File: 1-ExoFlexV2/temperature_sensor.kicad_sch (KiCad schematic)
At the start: 15 parts, among them J109 Jumper, J110 Jumper, U85 COMP, U86 COMP, U87 OR Gate

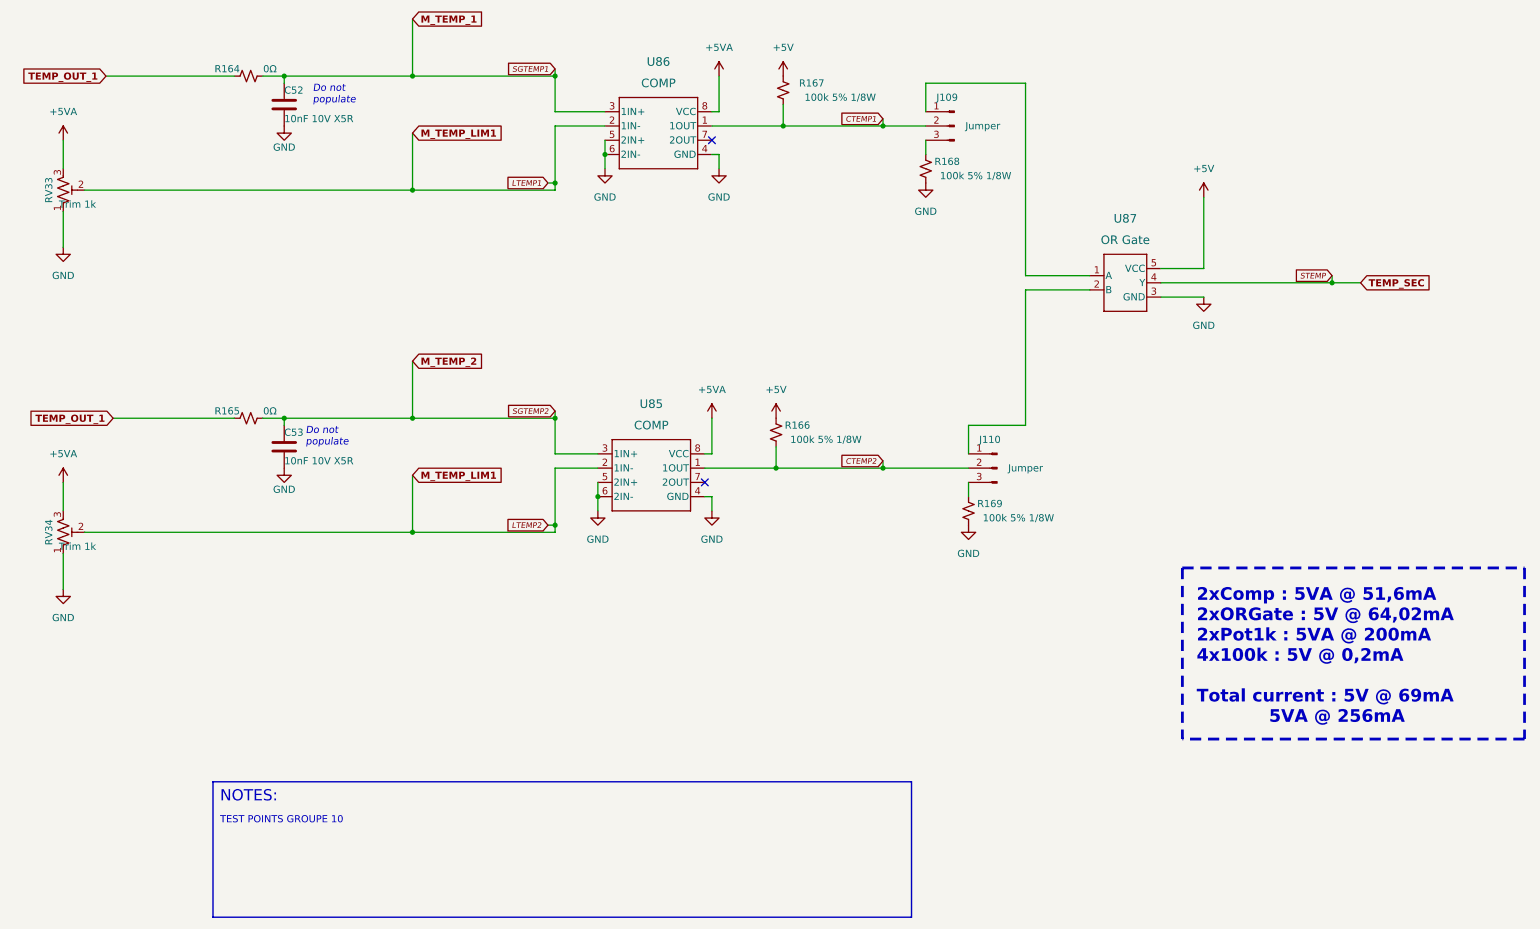
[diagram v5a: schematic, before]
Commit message: Finalisation 3
- Changement des régulateur de tension
- Retrait de test point inutile
- Changement de jumper mal positionner
- Ajout de Mounting holes et fiducial
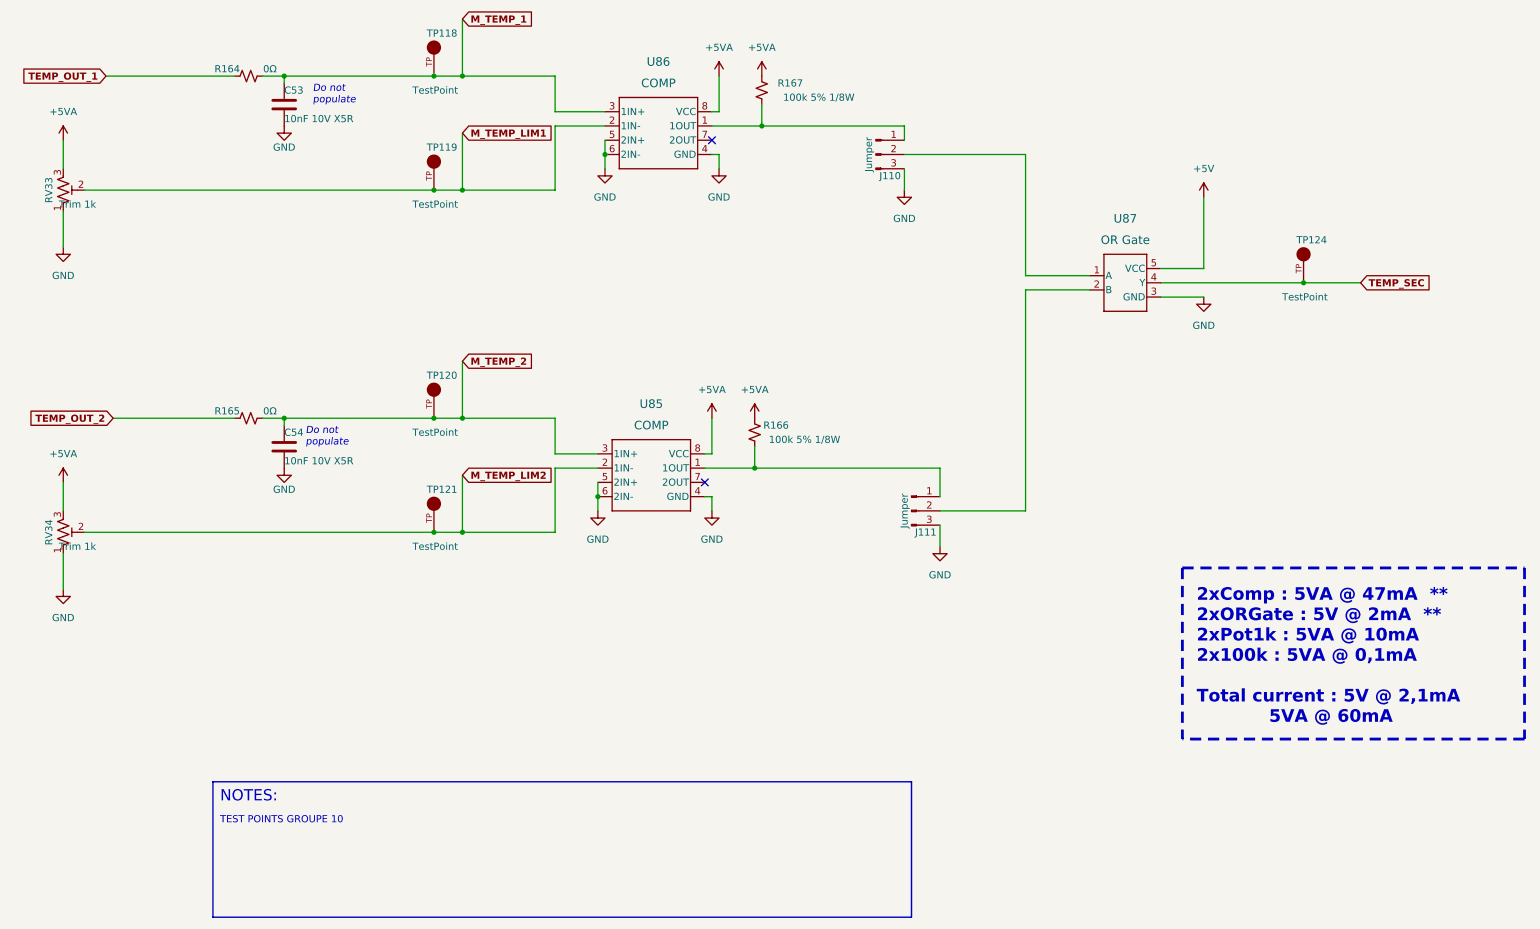
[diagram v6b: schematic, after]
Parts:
- removed C53: 10nF 10V X5R, Capacitor_SMD:C_01005_0402Metric, symbol Device:C
- removed R168, R169: 100k 5% 1/8W, Resistor_SMD:R_0805_2012Metric, symbol Device:R_Small_US
- added C54: 10nF 10V X5R, Capacitor_SMD:C_0603_1608Metric, symbol Device:C
- added TP118, TP119, TP120, TP121, TP124: TestPoint, FootPrint:KEYSTONE_5005, symbol SymLib:5005
- C53: renamed from C52; footprint Capacitor_SMD:C_01005_0402Metric -> Capacitor_SMD:C_0603_1608Metric; DESCRIPTION 10000 pF ±10% 10V Ceramic Capacitor X5R 01005 (0402 Metric) -> 10000 pF ±5% 10V Ceramic Capacitor U2J 0603 (1608 Metric); PACKAGE 01005 (0402 Metric) -> 0603 (1608 Metric); PART NUMBER GRM022R61A103KE19L -> GRM1857U1A103JA44D
- J110: renamed from J109; footprint Connector_PinSocket_2.54mm:PinSocket_1x03_P2.54mm_Vertical -> Connector_PinHeader_2.54mm:PinHeader_1x03_P2.54mm_Vertical
- J111: renamed from J110; footprint Connector_PinSocket_2.54mm:PinSocket_1x03_P2.54mm_Vertical -> Connector_PinHeader_2.54mm:PinHeader_1x03_P2.54mm_Vertical
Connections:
- net +5V: no longer R166.1, R167.1
- net +5VA: now also R166.1, R167.1
- net GND: now also J110.3 (Pin_3), J111.3 (Pin_3), C54.2
- net M_TEMP_1: now also TP118.TP
- net M_TEMP_2: now also C54.1, TP120.TP
- net TEMP_OUT_1: no longer R165.1
- net at J110.1 (Pin_1): now also R167.2, U86.1 (1OUT); no longer U87.1 (A)
- net at J111.1 (Pin_1): now also R166.2, U85.1 (1OUT); no longer U87.2 (B)
- removed net CTEMP1: J110.2 (Pin_2), R167.2, U86.1 (1OUT)
- removed net CTEMP2: J111.2 (Pin_2), R166.2, U85.1 (1OUT)
- net LTEMP1 renamed M_TEMP_LIM1
- net M_TEMP_LIM1: now also TP119.TP; no longer RV34.2, U85.2 (1IN-)
- net STEMP renamed TEMP_SEC
- net TEMP_SEC: now also TP124.TP
- new net: J110.2 (Pin_2), U87.1 (A)
- new net: J111.2 (Pin_2), U87.2 (B)
- new net M_TEMP_LIM2: RV34.2, TP121.TP, U85.2 (1IN-)
- new net TEMP_OUT_2: R165.1
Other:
- note added: "2xComp : 5VA @ 47mA ** 2xORGate : 5V @ 2mA ** 2xPot1k : 5VA @ 10mA 2x100k : 5VA @ 0,1mA Total current : 5V @ 2,1mA 5VA @ 60mA"
- note removed: "2xComp : 5VA @ 51,6mA 2xORGate : 5V @ 64,02mA 2xPot1k : 5VA @ 200mA 4x100k : 5V @ 0,2mA Total current : 5V @ 69mA 5VA @ 256mA"
- moved on the sheet: J110, J111, R166, R167

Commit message: Finalisation schéma FIN
- Changement des uméro pour les inverseurs
- Changement des connecteur et début de placement
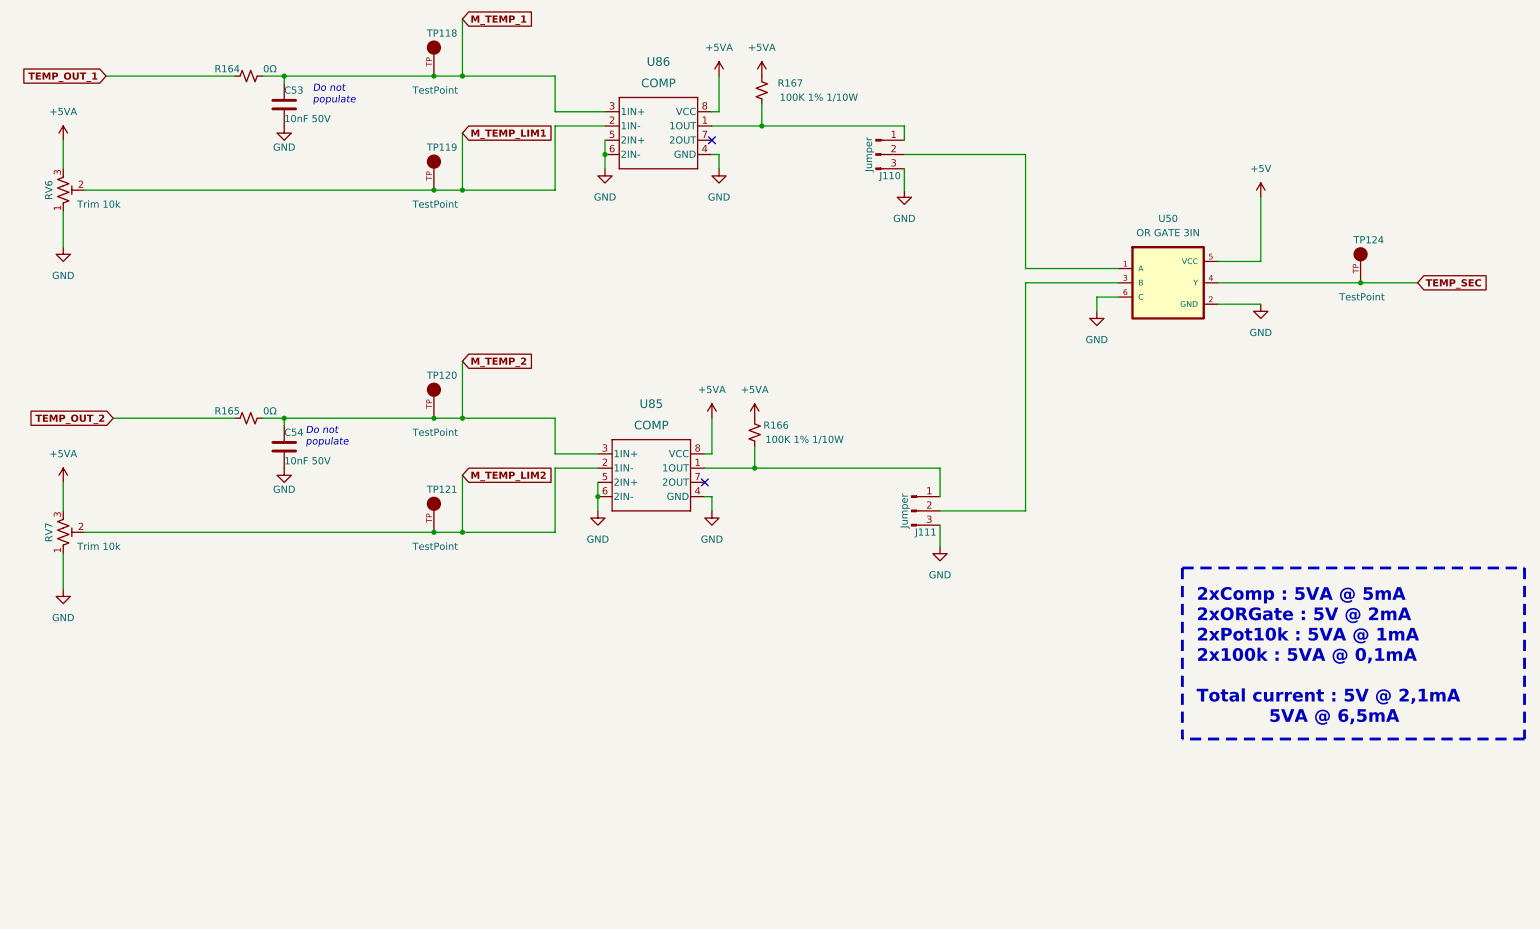
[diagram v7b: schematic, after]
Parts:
- removed RV33, RV34: Trim 1k, FootPrint:TRIM_3362P-1-102LF, symbol Device:R_Potentiometer_Trim_US
- removed U87: OR Gate, FootPrint:SOT95P270X145-5N, symbol SymLib:SN74LVC1G32DBVR
- added RV6, RV7: Trim 10k, FootPrint:TRIM_3362P-1-103LF, symbol Device:R_Potentiometer_Trim_US
- added U50: OR GATE 3IN, FootPrintLib:SOT95P280X145-6N, symbol SymLib:SN74LVC1G332DBVR
- C53, C54: value 10nF 10V X5R -> 10nF 50V; footprint Capacitor_SMD:C_0603_1608Metric -> Capacitor_SMD:C_0805_2012Metric; DESCRIPTION 10000 pF ±5% 10V Ceramic Capacitor U2J 0603 (1608 Metric) -> 10000 pF ±5% 50V Ceramic Capacitor C0G, NP0 0805 (2012 Metr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; PACKAGE 0603 (1608 Metric) -> 0805 (2012 Metric); PART NUMBER GRM1857U1A103JA44D -> GRM2195C1H103JA01D
- R166, R167: value 100k 5% 1/8W -> 100K 1% 1/10W; footprint Resistor_SMD:R_0805_2012Metric -> Resistor_SMD:R_0603_1608Metric; DESCRIPTION 100 kOhms ±5% 0.125W, 1/8W Chip Resistor 0805 (2012 Metric)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 -> 100 kOhms ±1% 0.1W, 1/10W Chip Resistor 0603 (1608 Metric) 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; PACKAGE 0805 (2012 Metric) -> 0603 (1608 Metric); PART NUMBER ERJ-6GEYJ104V -> ERJ-3EKF1003V
- TP118, TP119, TP120, TP121, TP124: NOTES (none) -> DO NOT POPULATE; PURCHASE-URL https://pricing.snapeda.com/search/part/5005/?ref=eda -> (none)
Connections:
- net +5V: now also U50.5 (VCC)
- net +5VA: now also RV6.3, RV7.3
- net GND: now also RV6.1, RV7.1, U50.2 (GND), U50.6 (C)
- net M_TEMP_LIM1: now also RV6.2
- net M_TEMP_LIM2: now also RV7.2
- net TEMP_SEC: now also U50.4 (Y)
- net at J110.2 (Pin_2): now also U50.1 (A)
- net at J111.2 (Pin_2): now also U50.3 (B)
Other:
- note added: "2xComp : 5VA @ 5mA 2xORGate : 5V @ 2mA 2xPot10k : 5VA @ 1mA 2x100k : 5VA @ 0,1mA Total current : 5V @ 2,1mA 5VA @ 6,5mA"
- note removed: "2xComp : 5VA @ 47mA ** 2xORGate : 5V @ 2mA ** 2xPot1k : 5VA @ 10mA 2x100k : 5VA @ 0,1mA Total current : 5V @ 2,1mA 5VA @ 60mA"
- note removed: "NOTES:"
- note removed: "TEST POINTS GROUPE 10"
- moved on the sheet: TP124

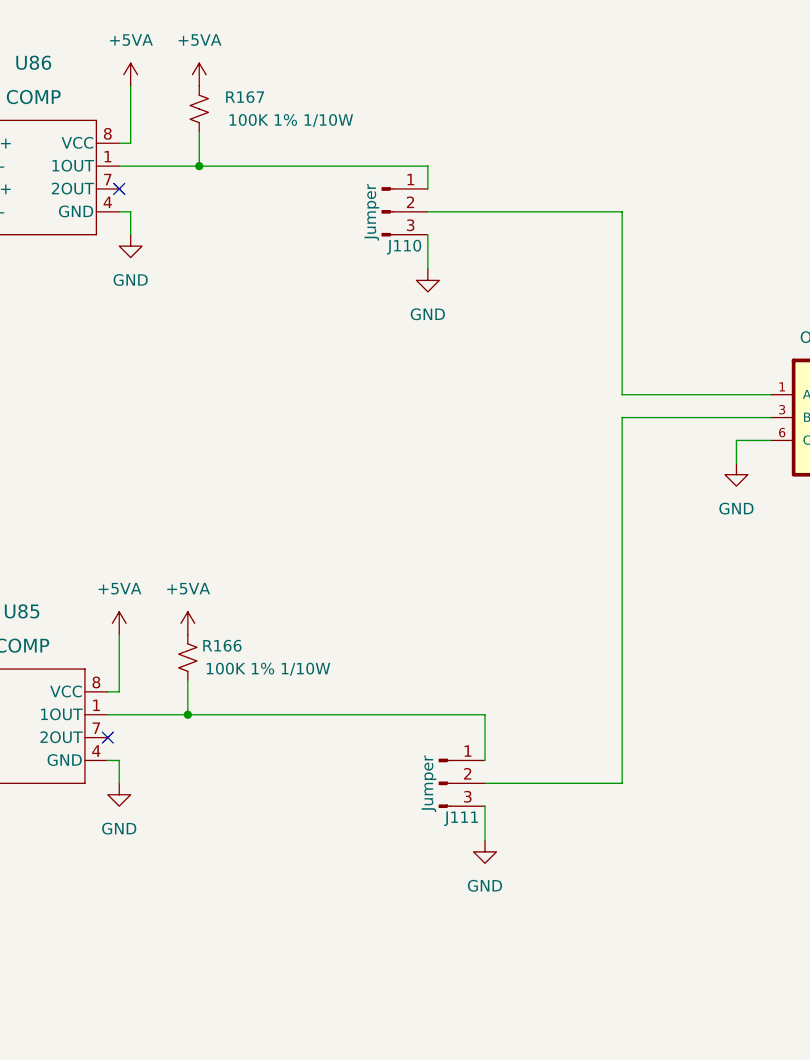
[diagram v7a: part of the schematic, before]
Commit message: Routage pour Review 1
- Replacement des test point pour faciliter le rework
- Correction des erreurs dans le BOM
-
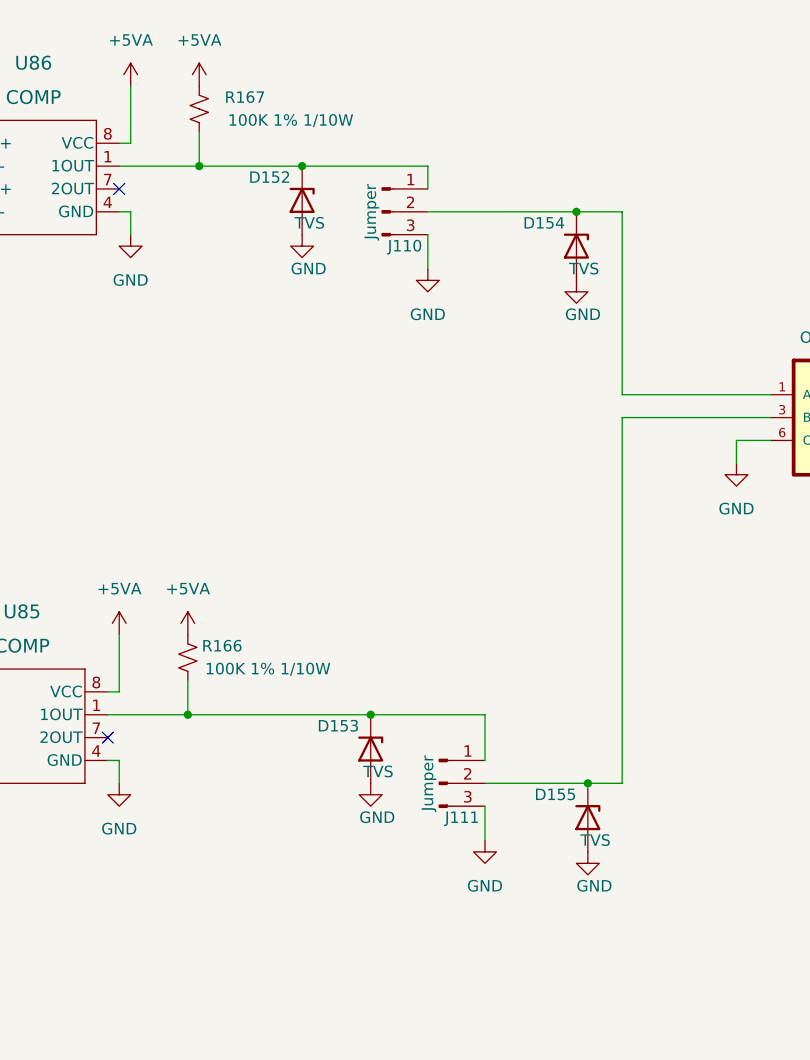
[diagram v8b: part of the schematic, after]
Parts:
- added D152, D153, D154, D155: TVS, FootPrint:DPY2_TEX, symbol Device:D_Zener
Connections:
- net GND: now also D152.2 (A), D153.2 (A), D154.2 (A), D155.2 (A)
- net at J111.1 (Pin_1), R166.2, U85.1 (1OUT): now also D153.1 (K)
- net at J110.1 (Pin_1), R167.2, U86.1 (1OUT): now also D152.1 (K)
- net at J110.2 (Pin_2), U50.1 (A): now also D154.1 (K)
- net at J111.2 (Pin_2), U50.3 (B): now also D155.1 (K)
